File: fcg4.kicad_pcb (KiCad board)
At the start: 4 copper layers, 35 x 35 mm, 99 parts, among them IC1 MP2456GJ-Z, IC2 MP2456GJ-Z, J1 USB4105-GF-A-120, J2 SM08B-SRSS-TB, U1 STM32G473CEUx, U2 ICM-42688-P, U23 SDA, U26 SCL, U31 9V, U4 AP2112K-3.3TRG1, U5 AP2112K-1.8TRG1, Y1 ECS-240-6-37B-7KM-TR

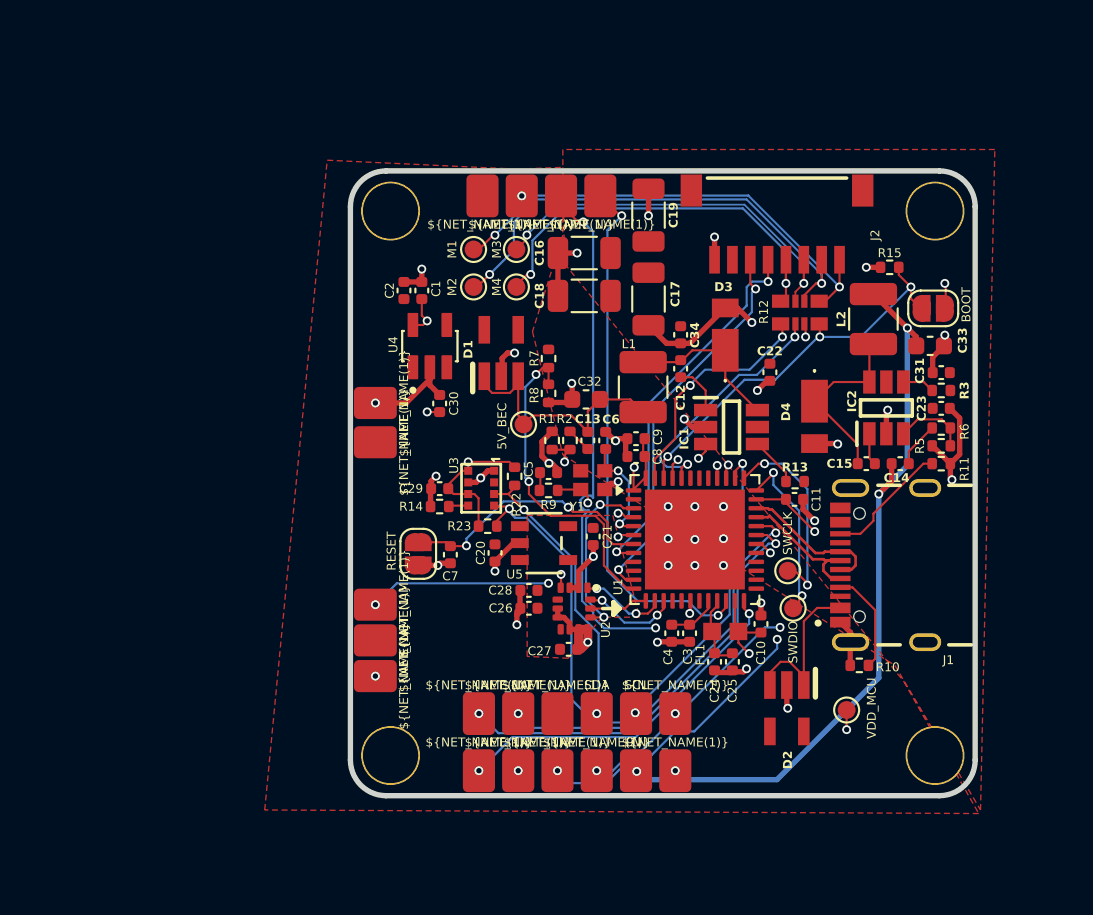
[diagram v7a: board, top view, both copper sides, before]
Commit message: reorganized everything and switched to 0603 as a minimum size
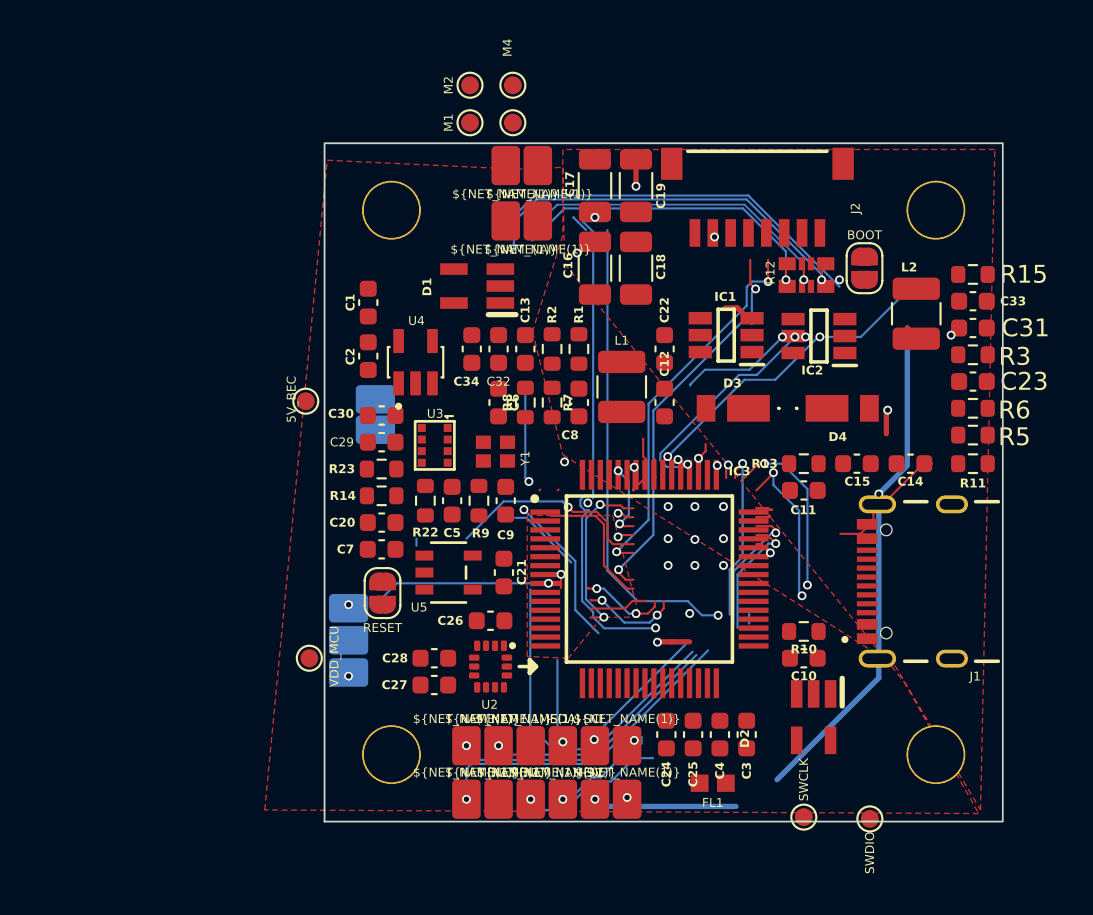
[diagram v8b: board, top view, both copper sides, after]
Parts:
- removed U1: STM32G473CEUx, fcg4_fp:QFN-48-1EP_7x7mm_P0.5mm_EP5.6x5.6mm
- added IC3: STM32G473RCT6, fcg4_fp:QFP50P1200X1200X160-64M, F.Cu at (16.2, 22.4)
- C1, C10, C11, C12, C13, C14, C15, C2, C20, C21, C22, C23, C24, C25, C26, C27, C28, C29, C3, C30, C31, C34, C4, C5, C6, C7, C8, C9: footprint Capacitor_SMD:C_0402_1005Metric -> Capacitor_SMD:C_0603_1608Metric
- R1, R10, R11, R13, R14, R15, R2, R22, R23, R3, R5, R6, R7, R8, R9: footprint Resistor_SMD:R_0402_1005Metric -> Resistor_SMD:R_0603_1608Metric
- U18, U19, U22, U24, U25: moved to B.Cu
- moved TP3 30.2 mm to (-2.80, 26.8)
- moved TP1 13.8 mm to (24.9, 35.7)
- moved TP2 12.6 mm to (28.6, 35.8)
- moved TP8 12.3 mm to (-3.00, 12.4)
- moved C34 11.7 mm to (6.30, 9.47), turned to -90 degrees
- moved TP5 11.3 mm to (6.20, -5.30)
- moved TP7 11.3 mm to (8.60, -5.30)
- moved FL1 8.53 mm to (19.8, 33.8)
- moved C9 8.08 mm to (8.20, 18.0), turned to -90 degrees
- moved C27 7.78 mm to (4.20, 28.3), turned to 180 degrees
- moved TP4 7.10 mm to (6.20, -3.20)
- moved TP6 7.10 mm to (8.60, -3.20)
- moved C17 7.02 mm to (13.2, 0.33)
- moved R23 6.75 mm to (1.25, 16.2)
- moved C20 6.57 mm to (1.25, 19.2), turned to 180 degrees
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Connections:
- net Net-(C13-Pad2) renamed /Power/RC_FB5V
- net Net-(C14-Pad2) renamed /Power/RC_FB9V
- net Net-(IC1-EN) renamed /Power/EN_5V
- net Net-(IC2-EN) renamed /Power/EN_9V
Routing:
- net GND: track 73.9 -> 35.9 mm, vias 44 -> 18
- net TX3: track 30.1 -> 0.00 mm, vias 2 -> 0
- net MOTOR2: track 25.5 -> 1.81 mm, vias 2 -> 1
- net MOTOR3: track 14.1 -> 37.5 mm, vias 2 -> 4
- net RX4: track 30.7 -> 8.31 mm, vias 3 -> 1
- net 5V5_BEC: track 15.1 -> 0.00 mm
- net MOTOR4: track 13.3 -> 0.00 mm, vias 2 -> 0
- net VOLTAGE_SENSOR: track 18.4 -> 5.38 mm, vias 2 -> 1
- net TX4: track 27.6 -> 18.0 mm, vias 3 -> 2
- net 5V_USB: track 9.61 -> 0.00 mm
- net /Power/SW_5V5: track 9.27 -> 0.00 mm
- net /Power/SW_9V: track 10.2 -> 1.21 mm
- net /Power/FB_5V5: track 10.8 -> 1.83 mm, vias 2 -> 0
- net TX1: track 24.5 -> 15.7 mm, vias 2 -> 1
- net /MCU/USB_DIFF+: track 8.19 -> 0.00 mm
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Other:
- board size 35 x 35 mm -> 38 x 38 mm
